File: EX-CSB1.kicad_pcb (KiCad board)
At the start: 4 copper layers, 65.9 x 52.9 mm, 103 parts, among them J101 MC 1,5/ 2-G-3,5, J103 MC 1,5/ 2-G-3,5, J105 STEMMA QT, J106 Conn_02x04, J107 Conn_01x10_f, J108 Conn_01x08_f, J110 MC 1,5/ 2-G-3,5, J111 Conn_01x04_f, J112 Conn_01x06_f, J113 Conn_01x08_f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

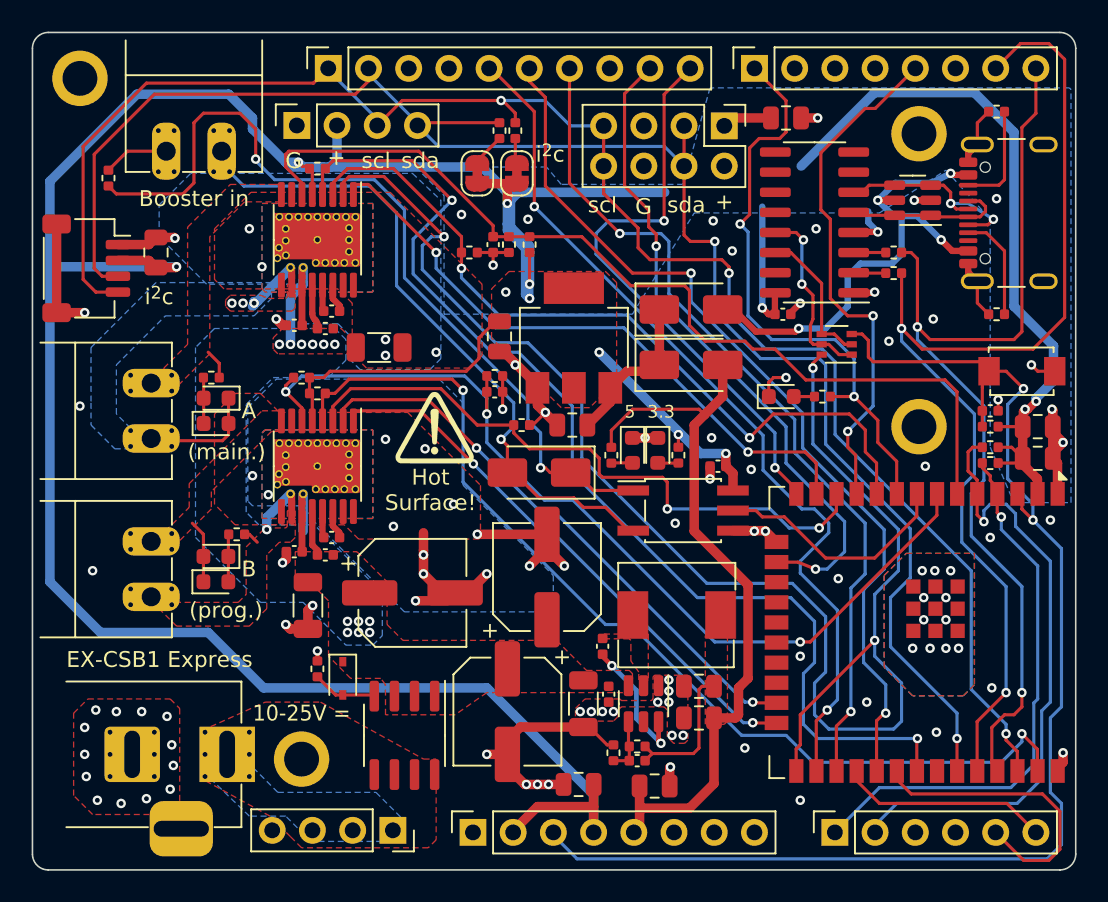
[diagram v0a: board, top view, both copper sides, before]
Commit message: Rev C
Removed dual I2C header to make room, Added booter common, fixed serial to conform with arduino standard, added option to provide vin_pin out by jumper (enabled by default) and added option to provide io_ref out by jumper (disabled by default).
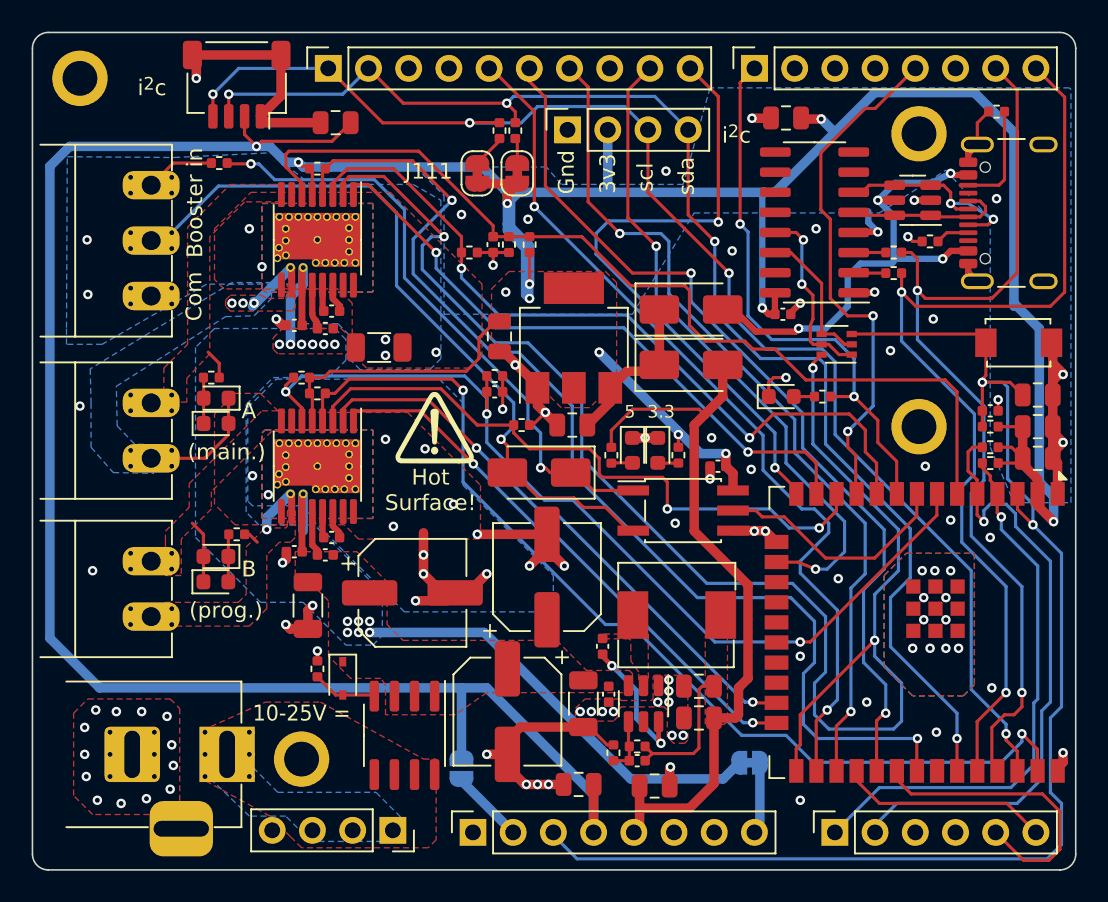
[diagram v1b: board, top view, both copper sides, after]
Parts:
- removed J106: Conn_02x04, Connector_PinHeader_2.54mm:PinHeader_2x04_P2.54mm_Vertical
- added C121: 10u, Capacitor_SMD:C_0805_2012Metric, F.Cu at (127.5, 81.5)
- added JP103: Jumper_2, Jumper:SolderJumper-2_P1.3mm_Bridged_RoundedPad1.0x1.5mm, B.Cu at (109.3, 104.7)
- added JP104: Jumper_2, Jumper:SolderJumper-2_P1.3mm_Open_RoundedPad1.0x1.5mm, B.Cu at (91.1, 105.1)
- J110: value MC 1,5/ 2-G-3,5 -> MC 1,5/ 3-G-3,5; footprint 0_my:PhoenixContact_MC_1,5_2-G-3.5_1x02_P3.50mm_Horizontal_edited -> Connector_Phoenix_MC:PhoenixContact_MC_1,5_3-G-3.5_1x03_P3.50mm_Horizontal
- moved J111 17.1 mm to (97.8, 64.8)
- moved J105 15.0 mm to (76.9, 61.9), turned to 180 degrees
- moved C115 14.0 mm to (83.2, 64.3), turned to 180 degrees
- moved R115 7.06 mm to (75.8, 66.8), turned to 0 degrees
- moved R119 6.23 mm to (120.7, 71.8)
- moved J110 3.45 mm to (71.5, 68.2), turned to -90 degrees
- moved JP101 2.53 mm to (94.6, 67.5)
- moved JP102 2.50 mm to (92.1, 67.5)
- moved SW101 1.81 mm to (126.3, 78.2)
- moved J101 1.25 mm to (71.5, 83.8)
- moved J103 1.25 mm to (71.5, 93.8)
- moved G*** 1.17 mm to (107.7, 93.9)
- moved R113 1.00 mm to (94.5, 64.8)
- moved R114 1.00 mm to (93.5, 64.8)
- turned C114 to 180 degrees
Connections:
- J108 pad 2: +3V3 -> /io_ref
- J108 pad 8: vin_pin -> /vin_pin
- J110 pad 1: /Booster-C -> /Booster-D
- J110 pad 2: /Booster-D -> /Booster-C
- J113 pad 7: /USB_TX -> /USB_RX
- J113 pad 8: /USB_RX -> /USB_TX
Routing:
- net VM: track 12.6 -> 40.3 mm
- net /sda: track 108.2 -> 85.2 mm, vias 2 -> 4
- net /scl: track 106.6 -> 86.2 mm, vias 3 -> 4
- net /opto_anode: track 53.3 -> 38.8 mm
- net +3V3: track 259.0 -> 269.3 mm
- net GND: track 88.0 -> 95.6 mm
- net /USB_TX: track 69.0 -> 61.5 mm
- net /Booster-C: track 40.4 -> 46.4 mm
- net /vin_pin: track 0.00 -> 5.10 mm
- net /io_ref: track 0.00 -> 4.73 mm
- net /cc1: track 6.77 -> 2.14 mm
- net /brake_d: track 36.3 -> 39.9 mm
- net /USB_RX: track 61.6 -> 58.2 mm
- net /reset_n: track 81.9 -> 85.0 mm
- net /d7: track 37.6 -> 35.2 mm
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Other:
- board text added: "3v3"
- board text added: "5v"
- board text added: "Com"
- board text added: "Gnd"
- board text added: "Rev C"
- board text added: "ioref"
- board text added: "rxd"
- board text added: "txd"
- board text added: "vin"
- board text removed: "3V3"
- board text removed: "5V"
- board text removed: "Common"
- board text removed: "Data"
- board text removed: "EX-CSB1 Express"
- board text removed: "G"
- board text removed: "GND"
- board text removed: "IO01"
- board text removed: "IO03"
- board text removed: "Rev B"
